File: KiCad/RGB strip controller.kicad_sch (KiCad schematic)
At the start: 17 parts, among them J1 USB_C_Receptacle_USB2.0, J2 Conn_01x03, SW1 SW_SPST, U1 ESP-01, U2 LM317_TO-220, U3 TC7SZ125FU

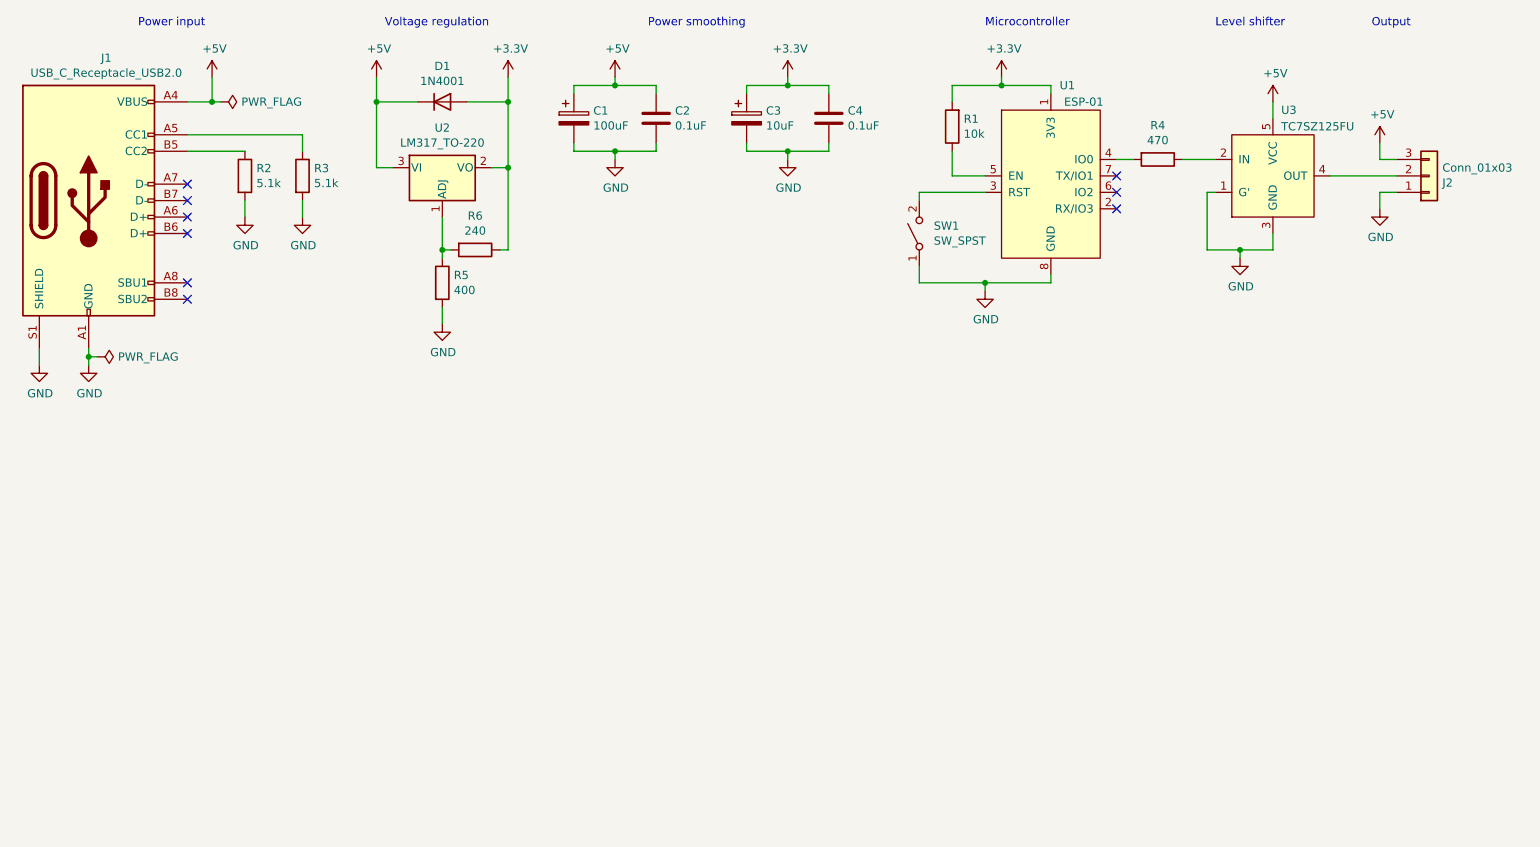
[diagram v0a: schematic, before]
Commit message: Add programming circuit to schematic
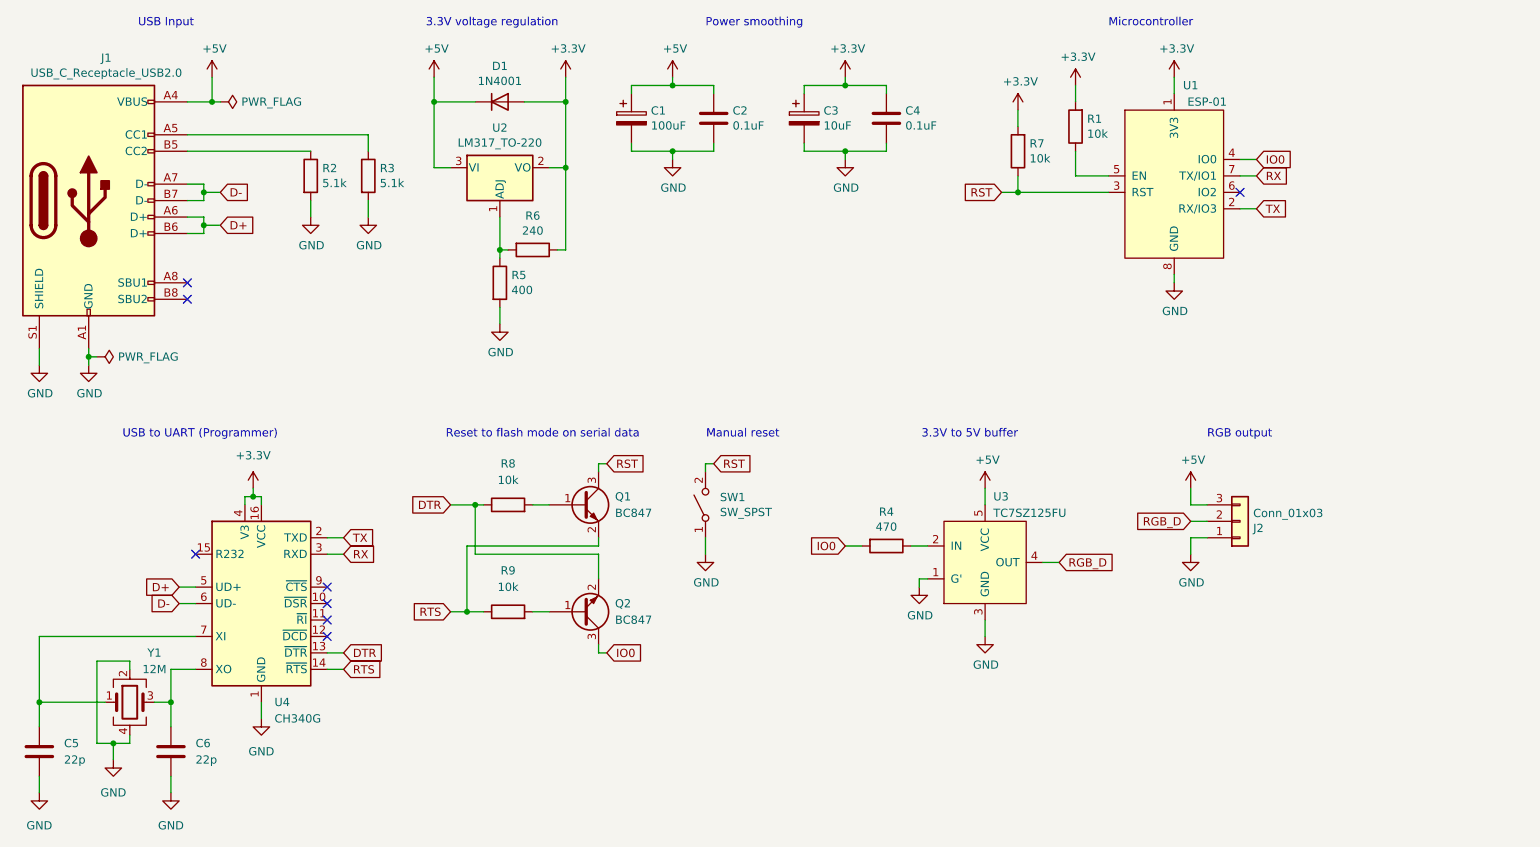
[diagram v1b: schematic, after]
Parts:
- added C5, C6: 22p, Capacitor_SMD:C_0603_1608Metric, symbol Device:C
- added Q1, Q2: BC847, Package_TO_SOT_SMD:SOT-23, symbol Transistor_BJT:BC847
- added R7, R8, R9: 10k, Resistor_SMD:R_0402_1005Metric, symbol Device:R
- added U4: CH340G, Package_SO:SOIC-16_3.9x9.9mm_P1.27mm, symbol Interface_USB:CH340G
- added Y1: 12M, Crystal:Crystal_SMD_3225-4Pin_3.2x2.5mm, symbol Device:Crystal_GND24
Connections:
- net +3V3: now also R7.2, U4.16 (VCC), U4.4 (V3)
- net GND: now also C5.2, C6.2, U4.1 (GND), Y1.2, Y1.4
- net TX: now reaches U1.2 (RX/IO3)
- net TX: now also U4.2 (TXD)
- net RST: now reaches SW1.2 (B), U1.3 (RST)
- net RST: now also Q1.3 (C), R7.1
- net IO0: now reaches R4.2, U1.4 (IO0)
- net IO0: now also Q2.3 (C)
- net RX: now reaches U1.7 (TX/IO1)
- net RX: now also U4.3 (RXD)
- net D+: now reaches J1.A6 (D+)
- net D+: now also J1.B6 (D+), U4.5 (UD+)
- net D-: now reaches J1.A7 (D-)
- net D-: now also J1.B7 (D-), U4.6 (UD-)
- net RGB_D: now reaches J2.2 (Pin_2), U3.4 (OUT)
- new net: C5.1, U4.7 (XI), Y1.1
- new net: C6.1, U4.8 (XO), Y1.3
- new net: Q1.1 (B), R8.2
- new net: Q2.1 (B), R9.2
- new net DTR: Q2.2 (E), R8.1, U4.13 (~{DTR})
- new net RTS: Q1.2 (E), R9.1, U4.14 (~{RTS})
- no-connect marks 9 -> 8
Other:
- note added: "3.3V to 5V buffer"
- note added: "3.3V voltage regulation"
- note added: "Manual reset"
- note added: "RGB output"
- note added: "Reset to flash mode on serial data"
- note added: "USB Input"
- note added: "USB to UART (Programmer)"
- note removed: "Level shifter"
- note removed: "Output"
- note removed: "Power input"
- note removed: "Voltage regulation"
- moved on the sheet: C1, C2, C3, C4, D1, J2, R1, R2, R3, R4, R5, R6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

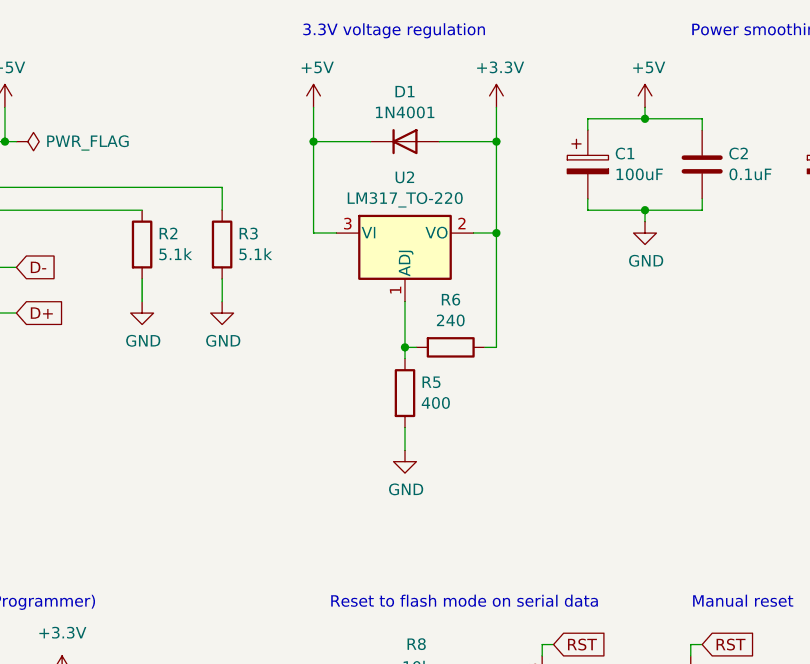
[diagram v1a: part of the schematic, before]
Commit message: Swap out LM317 for better LDO
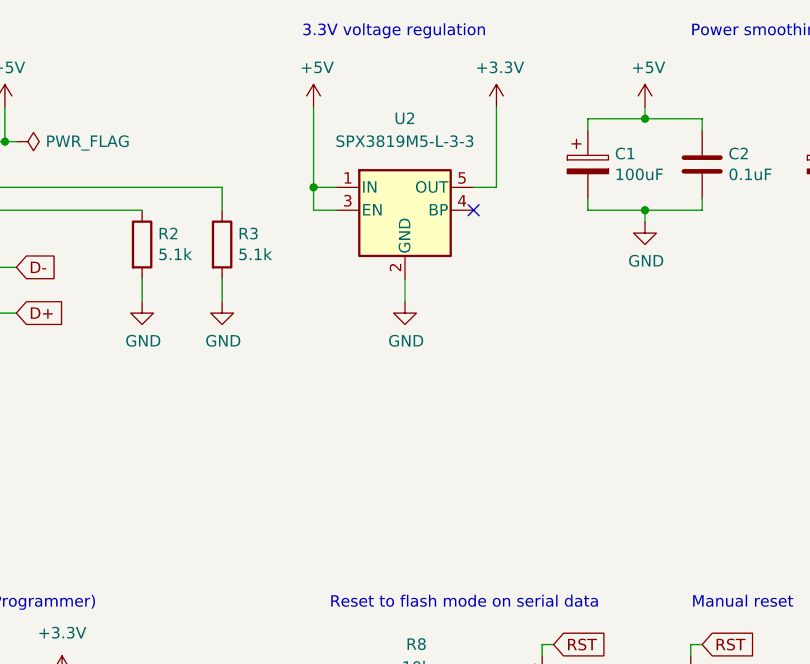
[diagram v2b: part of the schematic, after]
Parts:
- removed D1: 1N4001, Diode_SMD:D_SOD-123F, symbol Device:D
- removed R5: 400, Resistor_SMD:R_0402_1005Metric, symbol Device:R
- removed R6: 240, Resistor_SMD:R_0402_1005Metric, symbol Device:R
- removed U2: LM317_TO-220, Package_TO_SOT_THT:TO-220-3_Vertical, symbol Regulator_Linear:LM317_TO-220
- added U2: SPX3819M5-L-3-3, Package_TO_SOT_SMD:SOT-23-5, symbol Regulator_Linear:SPX3819M5-L-3-3
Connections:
- net +3V3: now also U2.5 (OUT)
- net +5V: now also U2.1 (IN), U2.3 (EN)
- net GND: now also U2.2 (GND)
- no-connect marks 8 -> 9

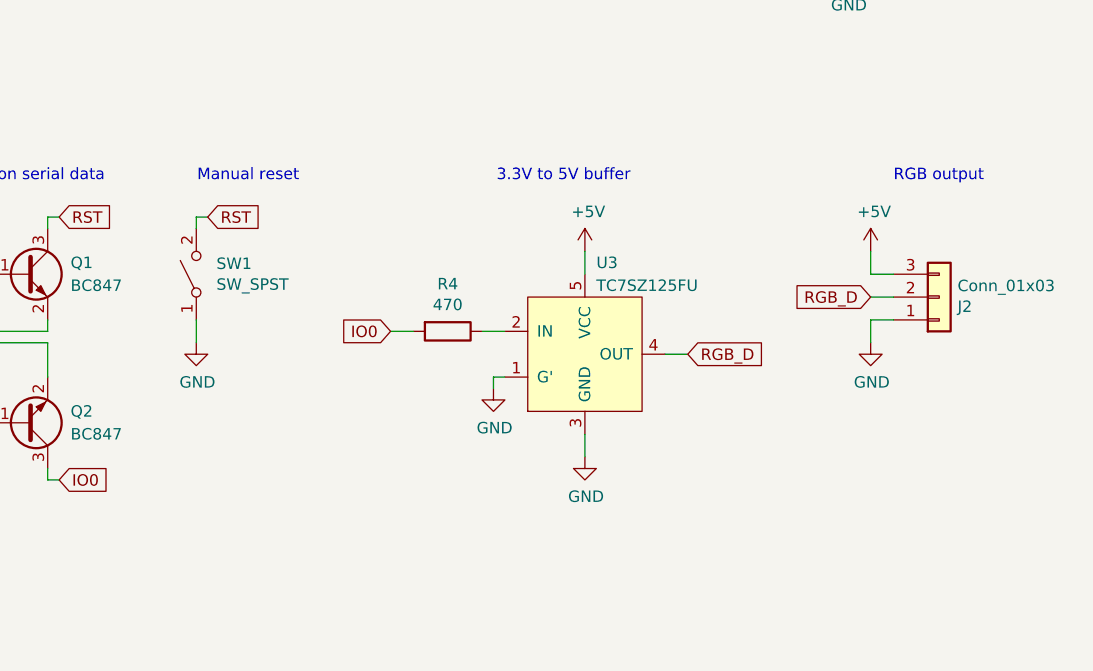
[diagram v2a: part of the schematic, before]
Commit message: Remove reset button
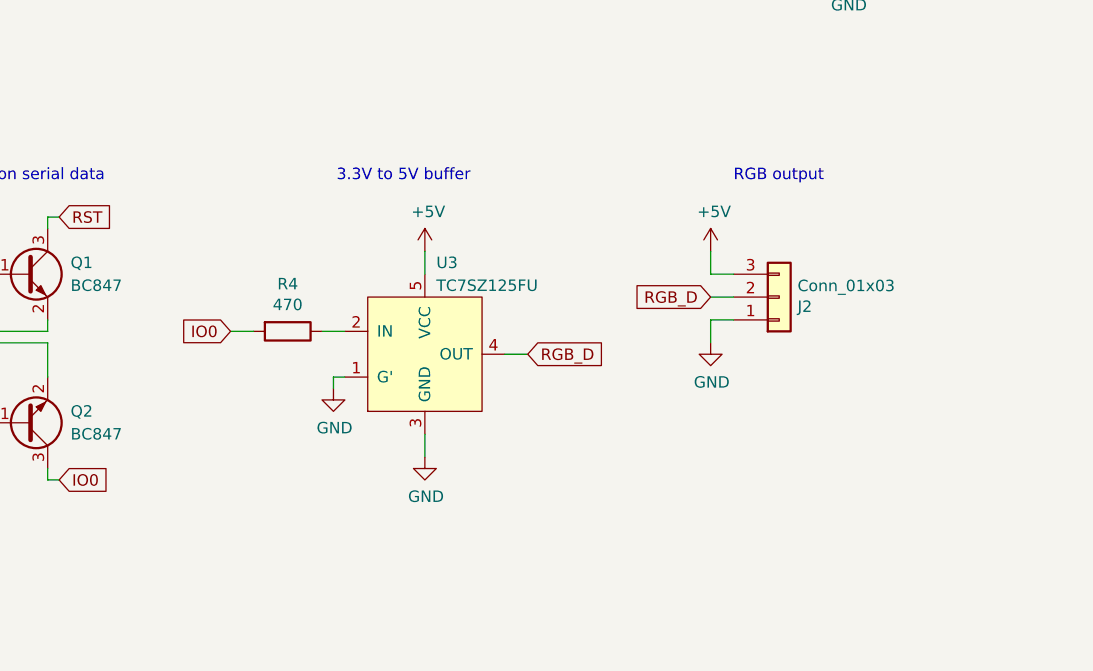
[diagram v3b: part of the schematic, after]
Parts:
- removed SW1: SW_SPST, Button_Switch_THT:SW_PUSH_6mm_H5mm, symbol Switch:SW_SPST
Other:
- note removed: "Manual reset"
- moved on the sheet: J2, R4, U3
